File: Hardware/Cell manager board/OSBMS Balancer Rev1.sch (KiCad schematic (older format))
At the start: 69 parts, among them P1 CONN_01X07, P2 EXT-TMP, P3 CONN_01X09, P4 CONN_01X09, P5 CONN_01X01, Q1 BSS138, Q2 BSS138, Q3 BSS138, Q4 BSS138, Q5 BSS138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

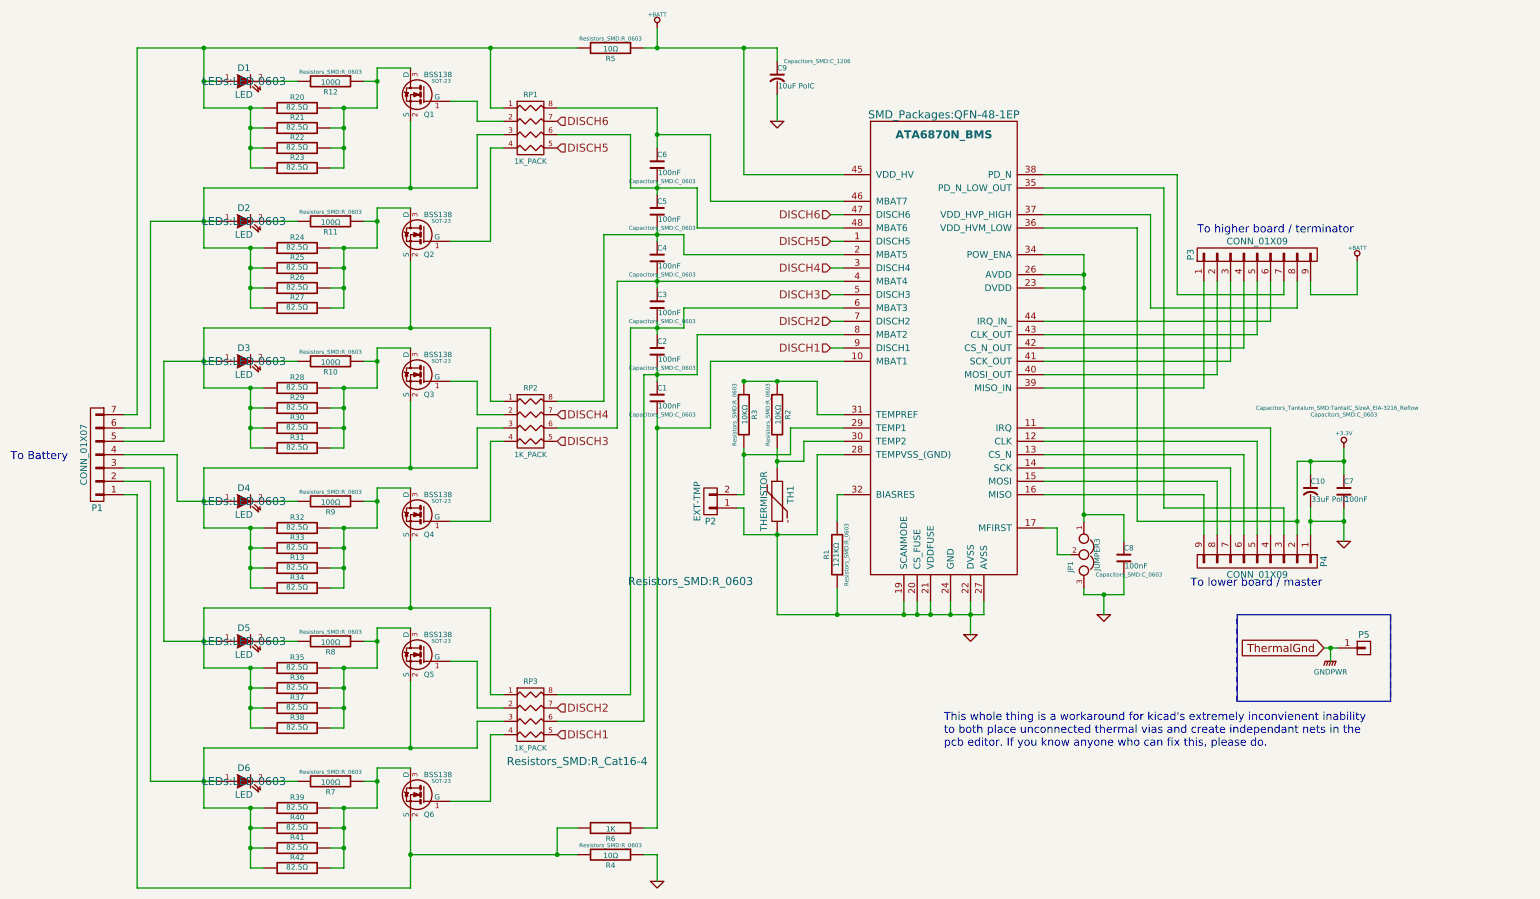
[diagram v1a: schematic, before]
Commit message: Finalised V1 for production
Finalised V1 for production. added hot symbol, moved mounting holes to
better location, fixed remaining drc error, and tiedied up silkscreen
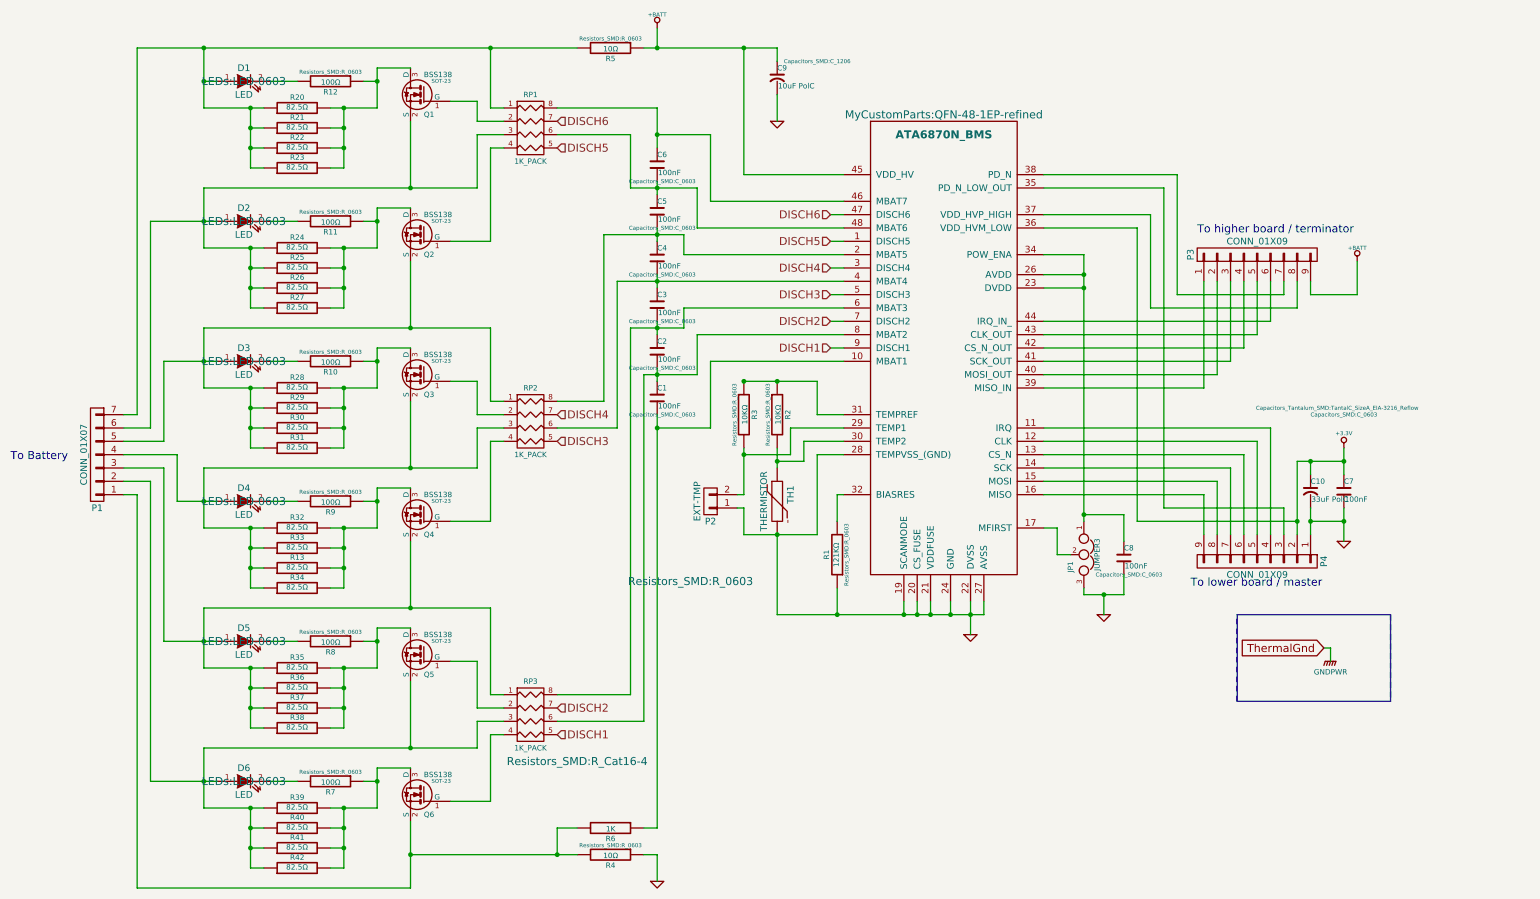
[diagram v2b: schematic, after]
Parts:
- removed P5: CONN_01X01, SMD_Packages:1Pin, symbol CONN_01X01
- P1: footprint Pin_Headers:Pin_Header_Angled_1x07 -> MyCustomParts:Shrouded_Header_Angled_1x07
- P2: footprint Pin_Headers:Pin_Header_Angled_1x02 -> Pin_Headers:Pin_Header_Straight_1x02
- P3, P4: footprint MasCustomParts:Connector_SMD_GH_SIDECONN_1X9_1.25MM_45515711ND -> MyCustomParts:Connector_SMD_GH_SIDECONN_1X9_1.25MM
- U1: footprint SMD_Packages:QFN-48-1EP -> MyCustomParts:QFN-48-1EP-refined
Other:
- note removed: "This whole thing is a workaround for kicad's extremely inconvienent inability\nto both place unconnected thermal vias and create independant nets in the \npcb editor. If you know anyone who can fix this, please do."
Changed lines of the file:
@@
 F 0 "U1" H 7550 4100 60  0001 C CNN
 F 1 "ATA6870N_BMS" H 7550 4200 60  0000 C CNB
-F 2 "SMD_Packages:QFN-48-1EP" H 7550 4350 60  0000 C CNN
+F 2 "MyCustomParts:QFN-48-1EP-refined" H 7550 4350 60  0000 C CNN
 F 3 "" H 7550 4200 60  0000 C CNN
 	1    7550 3050
@@
 $EndComp
 $Comp
-L +BATT #PWR1
+L +BATT #PWR01
 U 1 1 54188DB8
 P 5400 1100
-F 0 "#PWR1" H 5400 1050 20  0001 C CNN
+F 0 "#PWR01" H 5400 1050 20  0001 C CNN
 F 1 "+BATT" H 5400 1200 30  0000 C CNN
 F 2 "" H 5400 1100 60  0000 C CNN
@@
 $EndComp
 $Comp
-L GND #PWR7
+L GND #PWR02
 U 1 1 54188E78
 P 7750 5650
-F 0 "#PWR7" H 7750 5650 30  0001 C CNN
+F 0 "#PWR02" H 7750 5650 30  0001 C CNN
 F 1 "GND" H 7750 5580 30  0001 C CNN
 F 2 "" H 7750 5650 60  0000 C CNN
@@
 F 0 "P1" H 1200 4700 50  0000 C CNN
 F 1 "CONN_01X07" V 1300 4300 50  0000 C CNN
-F 2 "Pin_Headers:Pin_Header_Angled_1x07" H 950 6550 60  0001 C CNN
+F 2 "MyCustomParts:Shrouded_Header_Angled_1x07" H 950 6550 60  0001 C CNN
 F 3 "" H 1200 4300 60  0000 C CNN
 	1    1200 4300
@@
 To Battery
 $Comp
-L GND #PWR9
+L GND #PWR03
 U 1 1 54237CBF
 P 5400 7500
-F 0 "#PWR9" H 5400 7500 30  0001 C CNN
+F 0 "#PWR03" H 5400 7500 30  0001 C CNN
 F 1 "GND" H 5400 7430 30  0001 C CNN
 F 2 "" H 5400 7500 60  0000 C CNN
@@
 F 0 "P2" H 5800 4800 50  0000 C CNN
 F 1 "EXT-TMP" V 5900 4650 50  0000 C CNN
-F 2 "Pin_Headers:Pin_Header_Angled_1x02" H 6250 5400 60  0001 C CNN
+F 2 "Pin_Headers:Pin_Header_Straight_1x02" H 6250 5400 60  0001 C CNN
 F 3 "" H 5800 4650 60  0000 C CNN
 	1    5800 4650
@@
 $EndComp
 $Comp
-L GND #PWR2
+L GND #PWR04
 U 1 1 54268087
 P 6300 1800
-F 0 "#PWR2" H 6300 1800 30  0001 C CNN
+F 0 "#PWR04" H 6300 1800 30  0001 C CNN
 F 1 "GND" H 6300 1730 30  0001 C CNN
 F 2 "" H 6300 1800 60  0000 C CNN
@@
 F 0 "P3" H 9900 3300 50  0000 C CNN
 F 1 "CONN_01X09" V 10000 2800 50  0000 C CNN
-F 2 "MasCustomParts:Connector_SMD_GH_SIDECONN_1X9_1.25MM_45515711ND" V 12050 3200 60  0001 C CNN
+F 2 "MyCustomParts:Connector_SMD_GH_SIDECONN_1X9_1.25MM" V 12050 3200 60  0001 C CNN
 F 3 "" H 9900 2800 60  0000 C CNN
 	1    9900 2800
@@
 $EndComp
 $Comp
-L GND #PWR5
+L GND #PWR05
 U 1 1 54255D02
 P 10550 4950
-F 0 "#PWR5" H 10550 4950 30  0001 C CNN
+F 0 "#PWR05" H 10550 4950 30  0001 C CNN
 F 1 "GND" H 10550 4880 30  0001 C CNN
 F 2 "" H 10550 4950 60  0000 C CNN
@@
 $EndComp
 $Comp
-L +BATT #PWR3
+L +BATT #PWR06
 U 1 1 54257090
 P 10650 2850
-F 0 "#PWR3" H 10650 2800 20  0001 C CNN
+F 0 "#PWR06" H 10650 2800 20  0001 C CNN
 F 1 "+BATT" H 10650 2950 30  0000 C CNN
 F 2 "" H 10650 2850 60  0000 C CNN
@@
 $EndComp
 $Comp
-L GND #PWR6
+L GND #PWR07
 U 1 1 5425E157
 P 8750 5500
-F 0 "#PWR6" H 8750 5500 30  0001 C CNN
+F 0 "#PWR07" H 8750 5500 30  0001 C CNN
 F 1 "GND" H 8750 5430 30  0001 C CNN
 F 2 "" H 8750 5500 60  0000 C CNN
@@
 $EndComp
 $Comp
-L +3.3V #PWR4
+L +3.3V #PWR08
 U 1 1 54266B58
 P 10550 4250
-F 0 "#PWR4" H 10550 4210 30  0001 C CNN
+F 0 "#PWR08" H 10550 4210 30  0001 C CNN
 F 1 "+3.3V" H 10550 4360 30  0000 C CNN
 F 2 "" H 10550 4250 60  0000 C CNN
@@
 F 0 "P4" H 9900 5600 50  0000 C CNN
 F 1 "CONN_01X09" V 10000 5100 50  0000 C CNN
-F 2 "MasCustomParts:Connector_SMD_GH_SIDECONN_1X9_1.25MM_45515711ND" V 11200 4700 60  0001 C CNN
+F 2 "MyCustomParts:Connector_SMD_GH_SIDECONN_1X9_1.25MM" V 11200 4700 60  0001 C CNN
 F 3 "" H 9900 5100 60  0000 C CNN
 	1    9900 5100
@@
 $EndComp
 $Comp
-L GNDPWR #PWR8
+L GNDPWR #PWR09
 U 1 1 543C52AA
 P 10450 5850
-F 0 "#PWR8" H 10450 5900 40  0001 C CNN
+F 0 "#PWR09" H 10450 5900 40  0001 C CNN
 F 1 "GNDPWR" H 10450 5770 40  0000 C CNN
 F 2 "" H 10450 5850 60  0000 C CNN
@@
 Wire Notes Line
 	9750 6150 9750 5500
-Text Notes 7550 6500 0    60   ~ 0
-This whole thing is a workaround for kicad's extremely inconvienent inability\nto both place unconnected thermal vias and create independant nets in the \npcb editor. If you know anyone who can fix this, please do.
-$Comp
-L CONN_01X01 P5
-U 1 1 543D6344
-P 10700 5750
-F 0 "P5" H 10700 5850 50  0000 C CNN
-F 1 "CONN_01X01" V 10800 5750 50  0001 C CNN
-F 2 "SMD_Packages:1Pin" H 10700 5750 60  0001 C CNN
-F 3 "" H 10700 5750 60  0000 C CNN
-	1    10700 5750
-	1    0    0    -1
-$EndComp
-Wire Wire Line
-	10400 5750 10500 5750
-Wire Wire Line
-	10450 5750 10450 5850
-Connection ~ 10450 5750
 Wire Bus Line
 	10900 5500 9750 5500
@@
 Wire Bus Line
 	9750 5500 9750 6150
+Wire Wire Line
+	10450 5850 10450 5750
+Wire Wire Line
+	10450 5750 10400 5750
 $EndSCHEMATC
